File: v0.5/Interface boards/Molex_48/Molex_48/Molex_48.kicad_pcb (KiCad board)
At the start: 2 copper layers, 2 parts, among them J1 Conn_02x20_Counter_Clockwise, J2 500762-0482

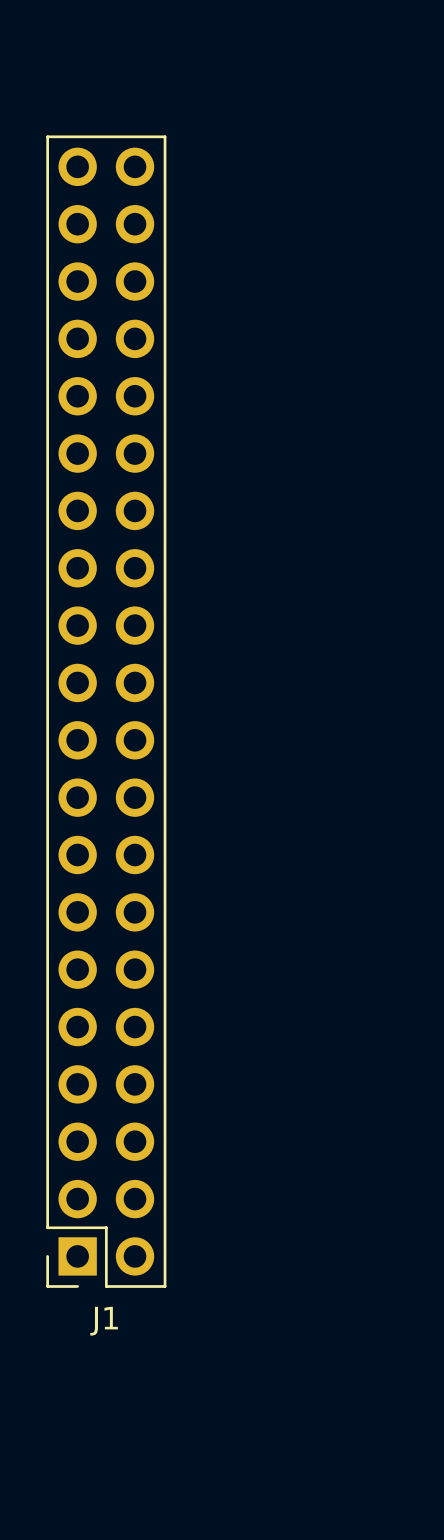
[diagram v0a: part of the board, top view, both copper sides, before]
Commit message: Update Molex_48.kicad_pcb
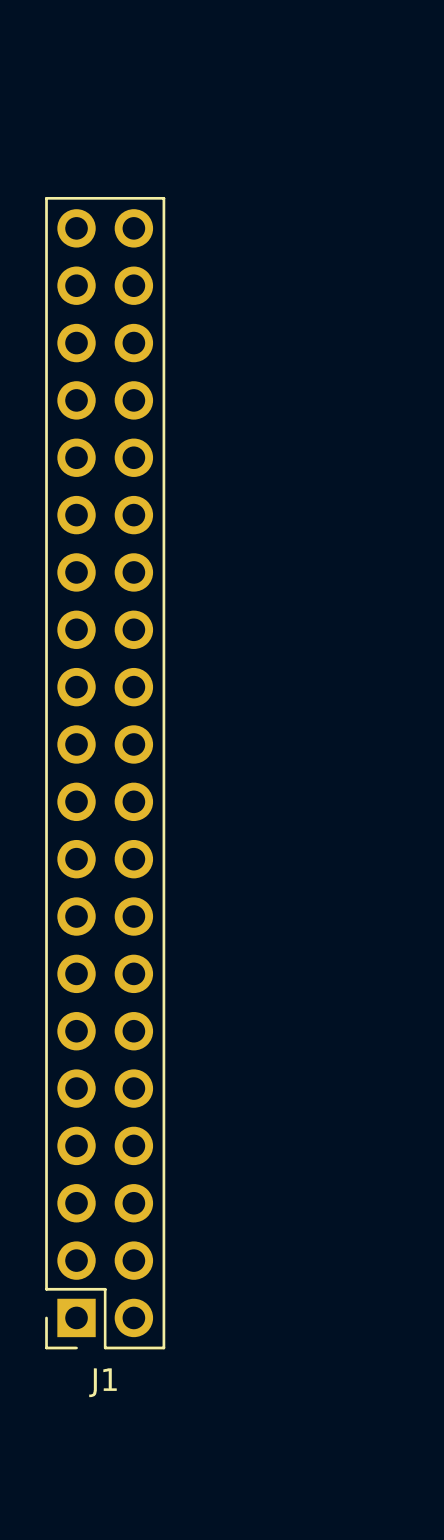
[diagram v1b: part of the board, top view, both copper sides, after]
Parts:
- moved J1 2.73 mm to (102.2, 120.6)
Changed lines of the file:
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@@
   )
   (footprint "Connector_PinSocket_2.54mm:PinSocket_2x20_P2.54mm_Vertical" (layer "F.Cu")
-    (at 102.26 117.875 180)
+    (at 102.21 120.6 180)
     (descr "Through hole straight socket strip, 2x20, 2.54mm pitch, double cols (from Kicad 4.0.7), script generated")
     (tags "Through hole socket strip THT 2x20 2.54mm double row")

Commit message: update
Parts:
- removed J1: Conn_02x20_Counter_Clockwise, Connector_PinSocket_2.54mm:PinSocket_2x20_P2.54mm_Vertical
- added J3: Conn_02x20_Odd_Even, Connector_PinSocket_2.54mm:PinSocket_2x20_P2.54mm_Vertical, F.Cu at (105.4, 120.6)
- J2: footprint SamacSys_Parts:5007620482 -> libs:5007620482
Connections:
- J2 pad A1: Injector_1_-_Pin_1-2 -> Injector_1
- J2 pad A2: Injector_2_-_Pin_1-2 -> Injector_2
- J2 pad A3: Injector_3_-_Pin_1-2 -> Injector_3
- J2 pad A4: Injector_4_-_Pin_1-2 -> Injector_4
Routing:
- net Injector_4: track 0.00 -> 62.3 mm
- net Injector_3: track 0.00 -> 48.9 mm
- net Injector_1: track 0.00 -> 26.7 mm
- net Injector_2: track 0.00 -> 24.3 mm
